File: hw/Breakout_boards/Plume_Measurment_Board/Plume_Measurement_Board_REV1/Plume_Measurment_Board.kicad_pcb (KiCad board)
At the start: 2 copper layers, 43 parts, among them J2 Conn_01x04, J3 Conn_Coaxial, J4 Conn_01x04, U2 LMP7721MA/NOPB, U3 LMP2022MA/NOPB, U4 AD8475ARMZ, U5 AD8475ARMZ, U6 TPS62153, U7 AD7176-2BRUZ

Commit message: Mirrored Layout Finish
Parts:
- added C24: .1pF, Capacitor_SMD:C_0402_1005Metric_Pad0.74x0.62mm_HandSolder, F.Cu at (206.2, 51.2)
- added C25: 1uF, Capacitor_SMD:C_0603_1608Metric_Pad1.08x0.95mm_HandSolder, B.Cu at (191.5, 49.3)
- added C26: 1uF, Capacitor_SMD:C_0805_2012Metric_Pad1.18x1.45mm_HandSolder, B.Cu at (187.8, 49.2)
- added C27: 1uF, Capacitor_SMD:C_0603_1608Metric_Pad1.08x0.95mm_HandSolder, B.Cu at (196.5, 51.7)
- added C28: 1uF, Capacitor_SMD:C_0805_2012Metric_Pad1.18x1.45mm_HandSolder, B.Cu at (200.7, 46.6)
- added C29: 1uF, Capacitor_SMD:C_0603_1608Metric_Pad1.08x0.95mm_HandSolder, B.Cu at (200.6, 51.6)
- added C30: 1uF, Capacitor_SMD:C_0805_2012Metric_Pad1.18x1.45mm_HandSolder, B.Cu at (196.5, 46.6)
- added C31: .1uF, Capacitor_SMD:C_0603_1608Metric_Pad1.08x0.95mm_HandSolder, F.Cu at (162.4, 49.3)
- added C32: 10uF, Capacitor_SMD:C_0805_2012Metric_Pad1.18x1.45mm_HandSolder, F.Cu at (162.8, 55.5)
- added C33: 100nF, Capacitor_SMD:C_0603_1608Metric_Pad1.08x0.95mm_HandSolder, F.Cu at (159.6, 55.5)
- added C34: 1uF, Capacitor_SMD:C_0603_1608Metric_Pad1.08x0.95mm_HandSolder, F.Cu at (161.5, 51.7)
- added C35: 680pF, Capacitor_SMD:C_0603_1608Metric_Pad1.08x0.95mm_HandSolder, F.Cu at (182.6, 45.6)
- added C36: 680pF, Capacitor_SMD:C_0603_1608Metric_Pad1.08x0.95mm_HandSolder, F.Cu at (182.5, 53.1)
- added C37: 1uF, Capacitor_SMD:C_0805_2012Metric_Pad1.18x1.45mm_HandSolder, F.Cu at (176.0, 52.3)
- added C38: 270pF, Capacitor_SMD:C_0603_1608Metric_Pad1.08x0.95mm_HandSolder, F.Cu at (180.6, 43.6)
- added C39: 270pF, Capacitor_SMD:C_0603_1608Metric_Pad1.08x0.95mm_HandSolder, F.Cu at (180.6, 47.0)
- added C40: 270pF, Capacitor_SMD:C_0603_1608Metric_Pad1.08x0.95mm_HandSolder, F.Cu at (180.6, 51.3)
- added C41: 270pF, Capacitor_SMD:C_0603_1608Metric_Pad1.08x0.95mm_HandSolder, F.Cu at (180.6, 54.7)
- added C42: 10uF, Capacitor_SMD:C_0805_2012Metric_Pad1.18x1.45mm_HandSolder, F.Cu at (174.5, 55.4)
- added C43: 100nF, Capacitor_SMD:C_0603_1608Metric_Pad1.08x0.95mm_HandSolder, F.Cu at (177.7, 55.4)
- added J5: Conn_Coaxial, Connector_Coaxial:SMA_Molex_73251-2120_EdgeMount_Horizontal, F.Cu at (80.6, 50.6)
- added R14: 1G, Resistor_SMD:R_2512_6332Metric_Pad1.40x3.35mm_HandSolder, F.Cu at (209.3, 50.2)
- added R15: 1000, Resistor_SMD:R_0603_1608Metric_Pad0.98x0.95mm_HandSolder, F.Cu at (196.1, 44.8)
- added R16: 1000, Resistor_SMD:R_0603_1608Metric_Pad0.98x0.95mm_HandSolder, F.Cu at (198.7, 46.1)
- added R17: 1000, Resistor_SMD:R_0603_1608Metric_Pad0.98x0.95mm_HandSolder, F.Cu at (195.3, 54.7)
- added R18: 1000, Resistor_SMD:R_0603_1608Metric_Pad0.98x0.95mm_HandSolder, F.Cu at (198.7, 52.0)
- added R19: 10, Resistor_SMD:R_0603_1608Metric_Pad0.98x0.95mm_HandSolder, F.Cu at (185.9, 51.9)
- added R20: 10, Resistor_SMD:R_0603_1608Metric_Pad0.98x0.95mm_HandSolder, F.Cu at (185.9, 54.1)
- added R5: 10, Resistor_SMD:R_0603_1608Metric_Pad0.98x0.95mm_HandSolder, F.Cu at (186.0, 44.2)
- added R6: 10, Resistor_SMD:R_0603_1608Metric_Pad0.98x0.95mm_HandSolder, F.Cu at (186.0, 46.5)
- added U10: LMP7721MA/NOPB, Amplifier_Texas_Instruments:M08A, F.Cu at (202.5, 49.5)
- added U11: LMP2022MA/NOPB, Amplifier_Texas_Instruments:M08A, F.Cu at (194.8, 49.5)
- added U12: AD7176-2BRUZ, ADC_Analog_Devices:RU_24_ADI, F.Cu at (168.9, 52.7)
- added U8: AD8475ARMZ, Buffer_Analog_Devices:RM_10_ADI, F.Cu at (189.5, 53.0)
- added U9: AD8475ARMZ, Buffer_Analog_Devices:RM_10_ADI, F.Cu at (189.6, 45.3)
- moved J3 135.4 mm to (215.9, 50.4), turned to 0 degrees
- moved C1 86.8 mm to (139.8, 77.4)
- moved C2 86.8 mm to (140.6, 71.9)
- moved J2 86.8 mm to (154.4, 73.1)
- moved L1 86.8 mm to (145.2, 78.0)
- moved R1 86.8 mm to (139.5, 79.2)
- moved U6 43.7 mm to (148.0, 47.3)
- moved C3 43.7 mm to (148.0, 51.4)
- moved J4 31.3 mm to (150.5, 39.5)
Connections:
- net /+OUT_1 renamed /E-Spray Plume Measurement 1/+OUT_1
- net /+OUT_2 renamed /E-Spray Plume Measurement 1/+OUT_2
- net /-OUT_1 renamed /E-Spray Plume Measurement 1/-OUT_1
- net /-OUT_2 renamed /E-Spray Plume Measurement 1/-OUT_2
- net /1_IN0.8+ renamed /E-Spray Plume Measurement 1/1_IN0.8+
- net /2_IN0.8+ renamed /E-Spray Plume Measurement 1/2_IN0.8+
- net /Amplified_Plume_1 renamed /E-Spray Plume Measurement 1/Amplified_Plume_1
- C10 pad 1: /+2.5V -> /E-Spray Plume Measurement 1/+2.5V
- C17 pad 1: /Plume -> /E-Spray Plume Measurement 1/Plume_1
- C18 pad 2: /+2.5V -> /E-Spray Plume Measurement 1/+2.5V
- C19 pad 1: /+2.5V -> /E-Spray Plume Measurement 1/+2.5V
- C20 pad 1: /+2.5V -> /E-Spray Plume Measurement 1/+2.5V
- C21 pad 2: /+2.5V -> /E-Spray Plume Measurement 1/+2.5V
- C22 pad 1: /+2.5V -> /E-Spray Plume Measurement 1/+2.5V
- C23 pad 2: /+2.5V -> /E-Spray Plume Measurement 1/+2.5V
- C4 pad 1: /+2.5V -> /E-Spray Plume Measurement 1/+2.5V
- C5 pad 2: /+2.5V -> /E-Spray Plume Measurement 1/+2.5V
- C6 pad 1: /+2.5V -> /E-Spray Plume Measurement 1/+2.5V
- C9 pad 2: /+2.5V -> /E-Spray Plume Measurement 1/+2.5V
- J2 pad 4: GND -> /PM_CS_1
- J3 pad 1: /Plume -> /E-Spray Plume Measurement 2/Plume_2
- J3 pad 2: /+2.5V -> /E-Spray Plume Measurement 2/+2.5V
- J4 pad 4: /PM_CS -> /PM_CS_2
- R13 pad 2: /Plume -> /E-Spray Plume Measurement 1/Plume_1
- U2 pad 1: /+2.5V -> /E-Spray Plume Measurement 1/+2.5V
- U2 pad 2: /+2.5V -> /E-Spray Plume Measurement 1/+2.5V
- U2 pad 7: /+2.5V -> /E-Spray Plume Measurement 1/+2.5V
- U2 pad 8: /Plume -> /E-Spray Plume Measurement 1/Plume_1
- U3 pad 3: /+2.5V -> /E-Spray Plume Measurement 1/+2.5V
- U3 pad 5: /+2.5V -> /E-Spray Plume Measurement 1/+2.5V
- U4 pad 1: /+2.5V -> /E-Spray Plume Measurement 1/+2.5V
- U4 pad 4: /+2.5V -> /E-Spray Plume Measurement 1/+2.5V
- U5 pad 1: /+2.5V -> /E-Spray Plume Measurement 1/+2.5V
- U5 pad 4: /+2.5V -> /E-Spray Plume Measurement 1/+2.5V
- U7 pad 14: /PM_CS -> /PM_CS_1
- U7 pad 4: /+2.5V -> /E-Spray Plume Measurement 1/+2.5V
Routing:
- net /E-Spray Plume Measurement 2/+2.5V: track 0.00 -> 215.4 mm, vias 0 -> 6
- net /E-Spray Plume Measurement 1/+2.5V: track 0.00 -> 215.4 mm, vias 0 -> 6
- net /+2.5V: track 181.5 -> 0.00 mm, vias 6 -> 0
- net GND: track 104.9 -> 211.7 mm, vias 6 -> 12
- net +5V: track 73.2 -> 146.1 mm, vias 5 -> 10
- net /E-Spray Plume Measurement 2/Amplified_Plume_2: track 0.00 -> 19.4 mm
- net Net-(U12-AIN3): track 0.00 -> 17.3 mm
- net Net-(U12-AIN2): track 0.00 -> 16.2 mm
- net Net-(U12-AIN0): track 0.00 -> 15.4 mm
- net Net-(U12-AIN1): track 0.00 -> 14.6 mm
- net /E-Spray Plume Measurement 2/Plume_2: track 0.00 -> 13.4 mm
- net /E-Spray Plume Measurement 1/Plume_1: track 0.00 -> 13.4 mm
- net /Plume: track 13.2 -> 0.00 mm
- net /E-Spray Plume Measurement 2/3_IN0.8+: track 0.00 -> 13.2 mm
- net Net-(U11A-INB-): track 0.00 -> 11.1 mm
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
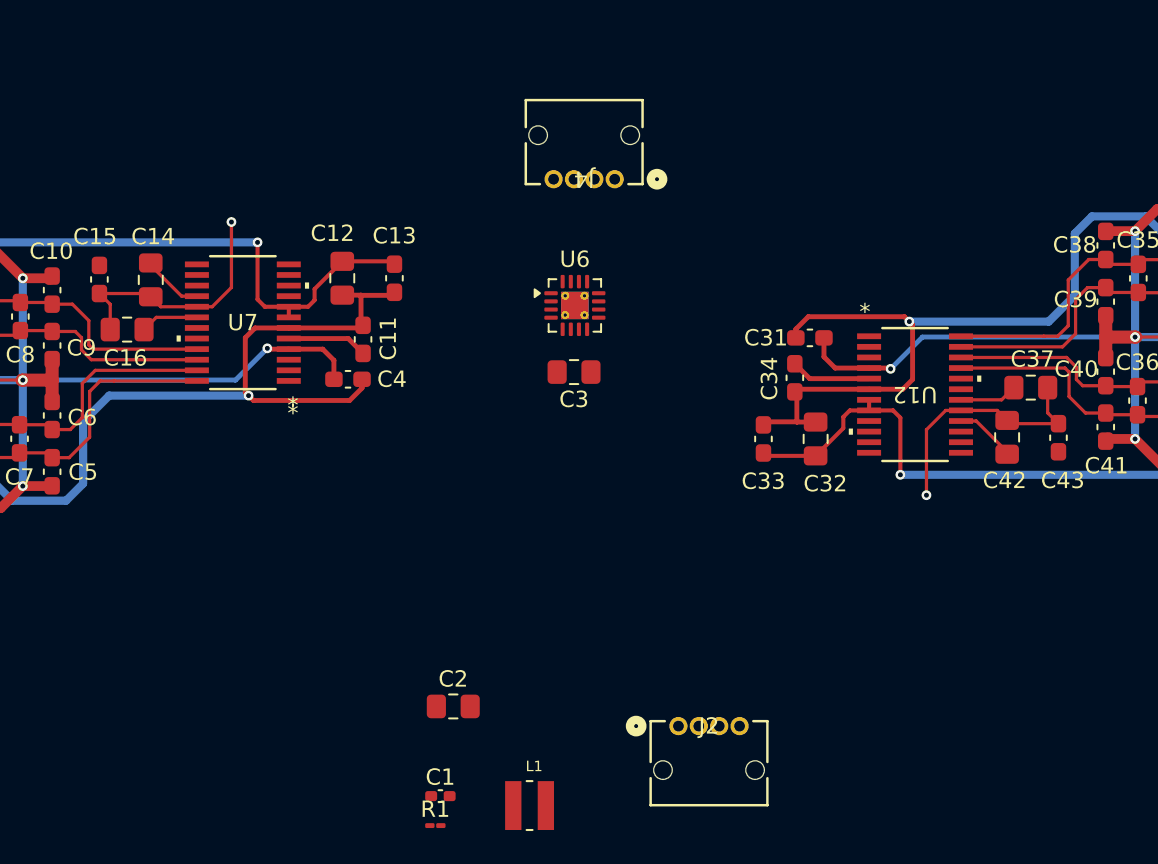
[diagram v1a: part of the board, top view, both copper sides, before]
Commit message: Mech Drawing in User.Drawings + Progress Routing 5V regulator
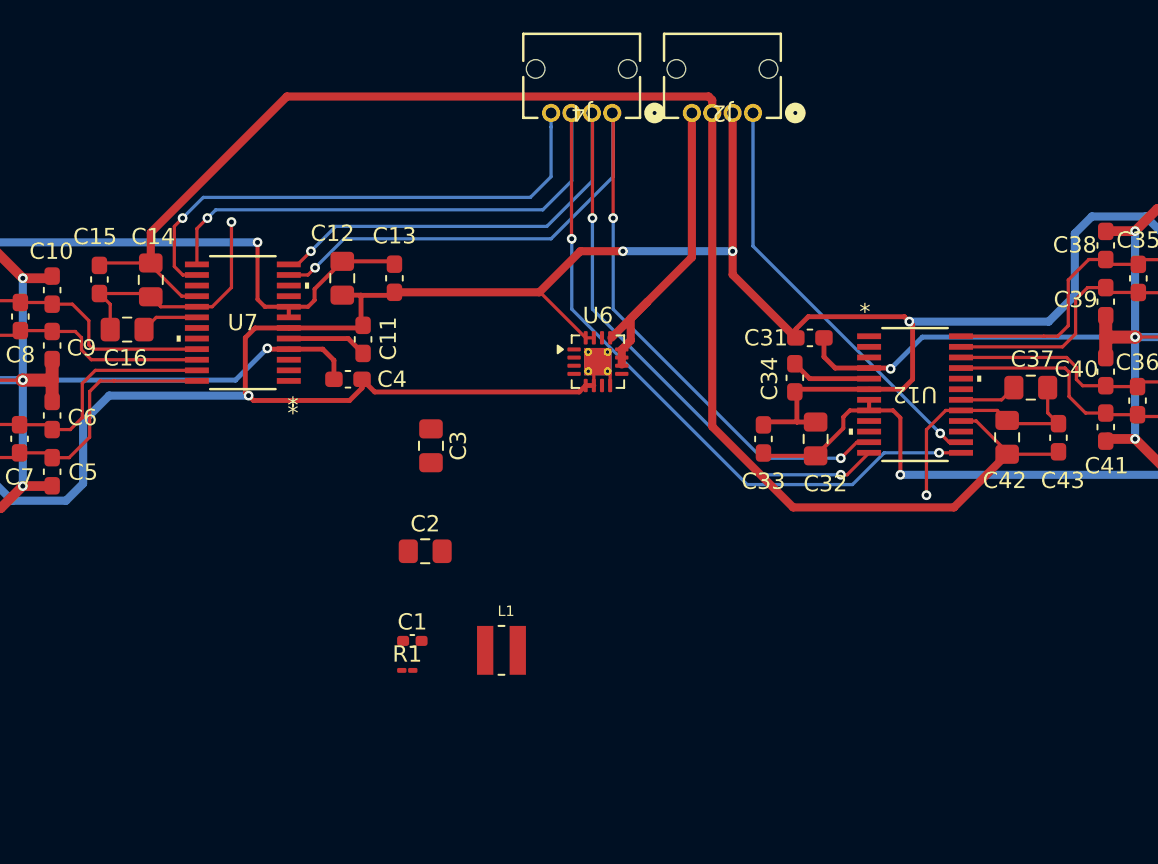
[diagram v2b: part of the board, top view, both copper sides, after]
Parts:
- moved J2 37.9 mm to (158.9, 35.5), turned to 180 degrees
- moved C3 9.87 mm to (139.2, 55.9), turned to -90 degrees
- moved C1 9.68 mm to (138.0, 67.8)
- moved C2 9.68 mm to (138.8, 62.4)
- moved L1 9.68 mm to (143.5, 68.4)
- moved R1 9.68 mm to (137.7, 69.7)
- moved J4 4.07 mm to (150.3, 35.5)
- moved U6 3.73 mm to (149.4, 50.7)
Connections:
- J2 pad 1: /+VBAT -> /PM_CS_2
- J2 pad 4: /PM_CS_1 -> /+VBAT
- J4 pad 1: /SPI1_MOSI -> /SPI1_MISO
- J4 pad 2: /SPI1_MISO -> /SPI1_MOSI
- J4 pad 4: /PM_CS_2 -> /PM_CS_1
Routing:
- net +3V3: track 7.52 -> 95.3 mm
- net /SPI1_SCK: track 0.00 -> 71.8 mm, vias 0 -> 3
- net GND: track 211.7 -> 270.6 mm, vias 12 -> 14
- net /SPI1_MOSI: track 0.00 -> 58.7 mm, vias 0 -> 3
- net /SPI1_MISO: track 0.00 -> 58.3 mm, vias 0 -> 3
- net /PM_CS_1: track 0.00 -> 32.4 mm, vias 0 -> 1
- net /PM_CS_2: track 0.00 -> 25.9 mm, vias 0 -> 1
- net /+VBAT: track 0.00 -> 20.3 mm

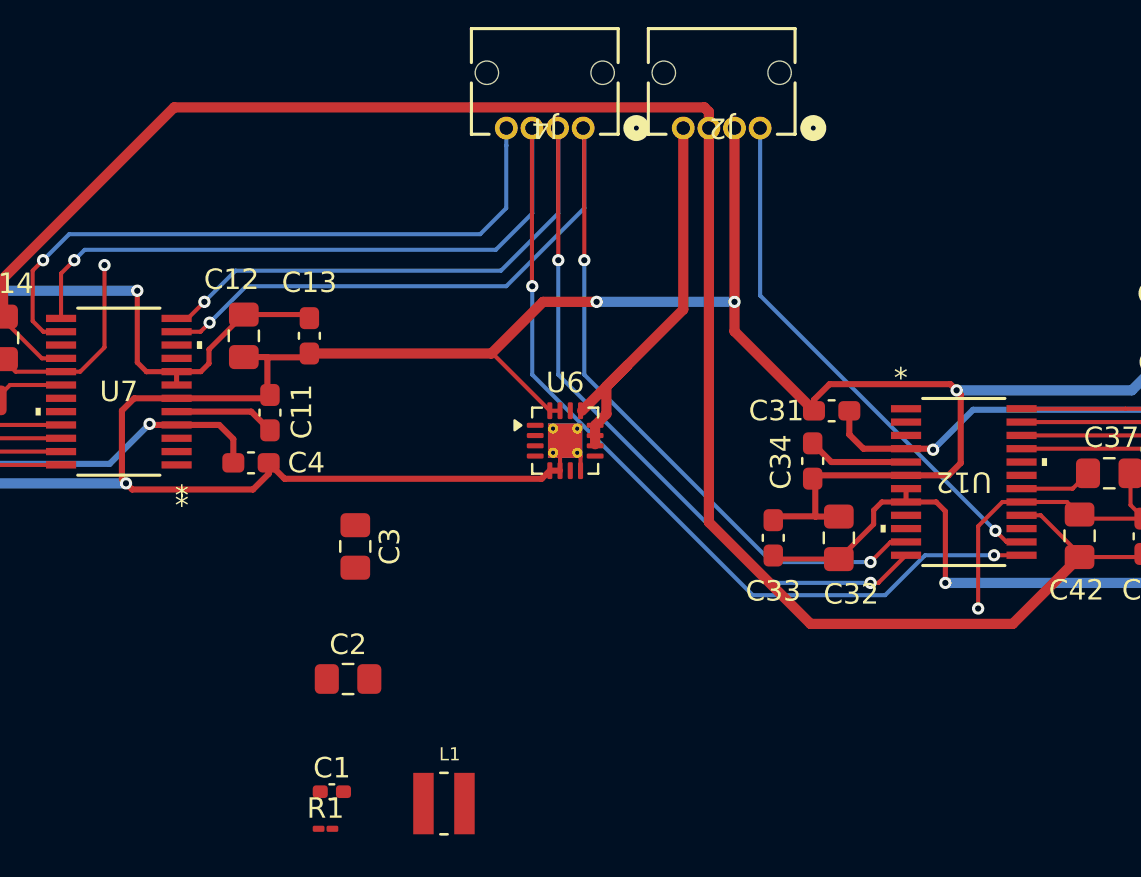
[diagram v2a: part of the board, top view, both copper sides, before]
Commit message: Finished Routing Voltage Regulator
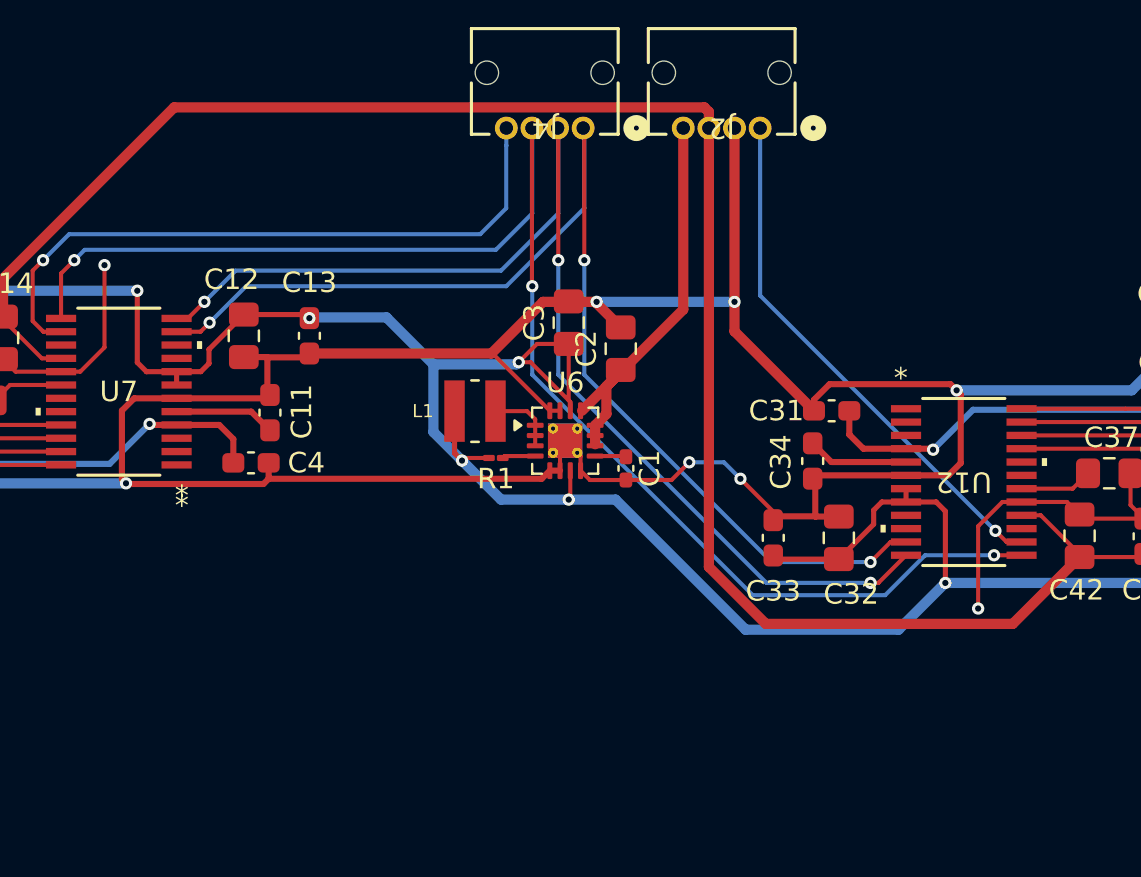
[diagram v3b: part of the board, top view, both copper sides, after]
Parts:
- moved C1 21.3 mm to (152.4, 52.1), turned to -90 degrees
- moved C2 20.9 mm to (152.1, 46.2), turned to 90 degrees
- moved R1 19.9 mm to (146.1, 51.6), turned to 180 degrees
- moved L1 19.2 mm to (145.0, 49.3), turned to 180 degrees
- moved C3 15.1 mm to (149.6, 45.0), turned to 90 degrees
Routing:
- net +5V: track 146.1 -> 205.3 mm, vias 10 -> 14
- net GND: track 270.6 -> 283.4 mm, vias 14 -> 16
- net Net-(L1-Pad1): track 0.00 -> 3.64 mm
- net Net-(U6-PG): track 0.00 -> 1.62 mm
- net Net-(U6-SS/TR): track 0.00 -> 1.52 mm
- net +3V3: track 95.3 -> 96.6 mm

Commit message: Edge Cuts Playing Around
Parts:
- added H1: MountingHole, MountingHole:MountingHole_3.5mm, F.Cu at (84.6, 30.5)
- added H2: MountingHole, MountingHole:MountingHole_3.5mm, F.Cu at (96.3, 65.0)
- added H3: MountingHole, MountingHole:MountingHole_3.5mm, F.Cu at (217.9, 38.9)
- added H4: MountingHole, MountingHole:MountingHole_3.5mm, F.Cu at (218.2, 62.5)
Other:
- board outline added: 131 x 18.7 mm

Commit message: Edge Cuts + Dimension Wor + Awaiting Dimension Approval
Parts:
- removed H1, H2, H3, H4: MountingHole, MountingHole:MountingHole_3.5mm
- moved C10 2.05 mm to (117.8, 45.4)
- moved C11 2.05 mm to (136.8, 48.4)
- moved C12 2.05 mm to (135.6, 44.6)
- moved C13 2.05 mm to (138.8, 44.6)
- moved C14 2.05 mm to (123.8, 44.7)
- moved C16 2.05 mm to (122.4, 47.8)
- moved C17 2.05 mm to (92.1, 48.9)
- moved C18 2.05 mm to (110.5, 50.9)
- moved C20 2.05 mm to (101.9, 48.4)
- moved C21 2.05 mm to (97.7, 53.5)
- moved C5 2.05 mm to (117.8, 56.5)
- moved C6 2.05 mm to (117.8, 53.1)
- moved C7 2.05 mm to (115.8, 54.5)
- moved C8 2.05 mm to (115.8, 47.0)
- moved J5 2.05 mm to (82.4, 49.7)
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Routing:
- net /SPI1_MISO: track 58.3 -> 56.6 mm
- net /SPI1_SCK: track 71.8 -> 70.1 mm
- net /SPI1_MOSI: track 58.7 -> 57.0 mm
- net GND: track 283.4 -> 281.7 mm
- net +5V: track 205.3 -> 203.7 mm
- net /PM_CS_1: track 32.4 -> 30.8 mm
- net +3V3: track 96.6 -> 95.3 mm
- net /E-Spray Plume Measurement 2/+2.5V: vias 6 -> 10
- added copper zone on F.Cu, net (none)
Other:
- board size 131 x 18.7 mm -> 140.3 x 38.3 mm

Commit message: Very interesting shape of board
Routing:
- added copper zone on B.Cu, net (none)
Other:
- outline, holes or cut-outs redrawn

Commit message: Hardware Debug Software Changes + New Mounting Holes for the Plume Measurement Board
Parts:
- added H1: MountingHole, MountingHole:MountingHole_2.5mm, F.Cu at (92.1, 62.2)
- added H2: MountingHole, MountingHole:MountingHole_2.5mm, F.Cu at (216.2, 62.5)
- added H3: MountingHole, MountingHole:MountingHole_2.5mm, F.Cu at (82.3, 30.5)
- added H4: MountingHole, MountingHole:MountingHole_2.5mm, F.Cu at (216.3, 39.6)
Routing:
- net /E-Spray Plume Measurement 2/+2.5V: vias 10 -> 6

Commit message: DRC Pass / Omitted A lot of Pointless Errors
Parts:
- moved C2 0.42 mm to (152.7, 45.1)
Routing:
- net GND: track 281.7 -> 275.9 mm, vias 16 -> 64
- net /SPI1_SCK: track 70.1 -> 69.3 mm
- added copper zone on B.Cu, net GND
- added copper zone on F.Cu, net GND
- removed copper zone on B.Cu, net (none)
- removed copper zone on F.Cu, net (none)
